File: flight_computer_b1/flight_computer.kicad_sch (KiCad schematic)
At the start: 11 parts, among them J1 DB25_Socket, J2 DB25_Socket, J3 Conn_01x03, J4 Screw_Terminal_01x02, J5 Pi Connector, J6 Conn_02x02_Odd_Even

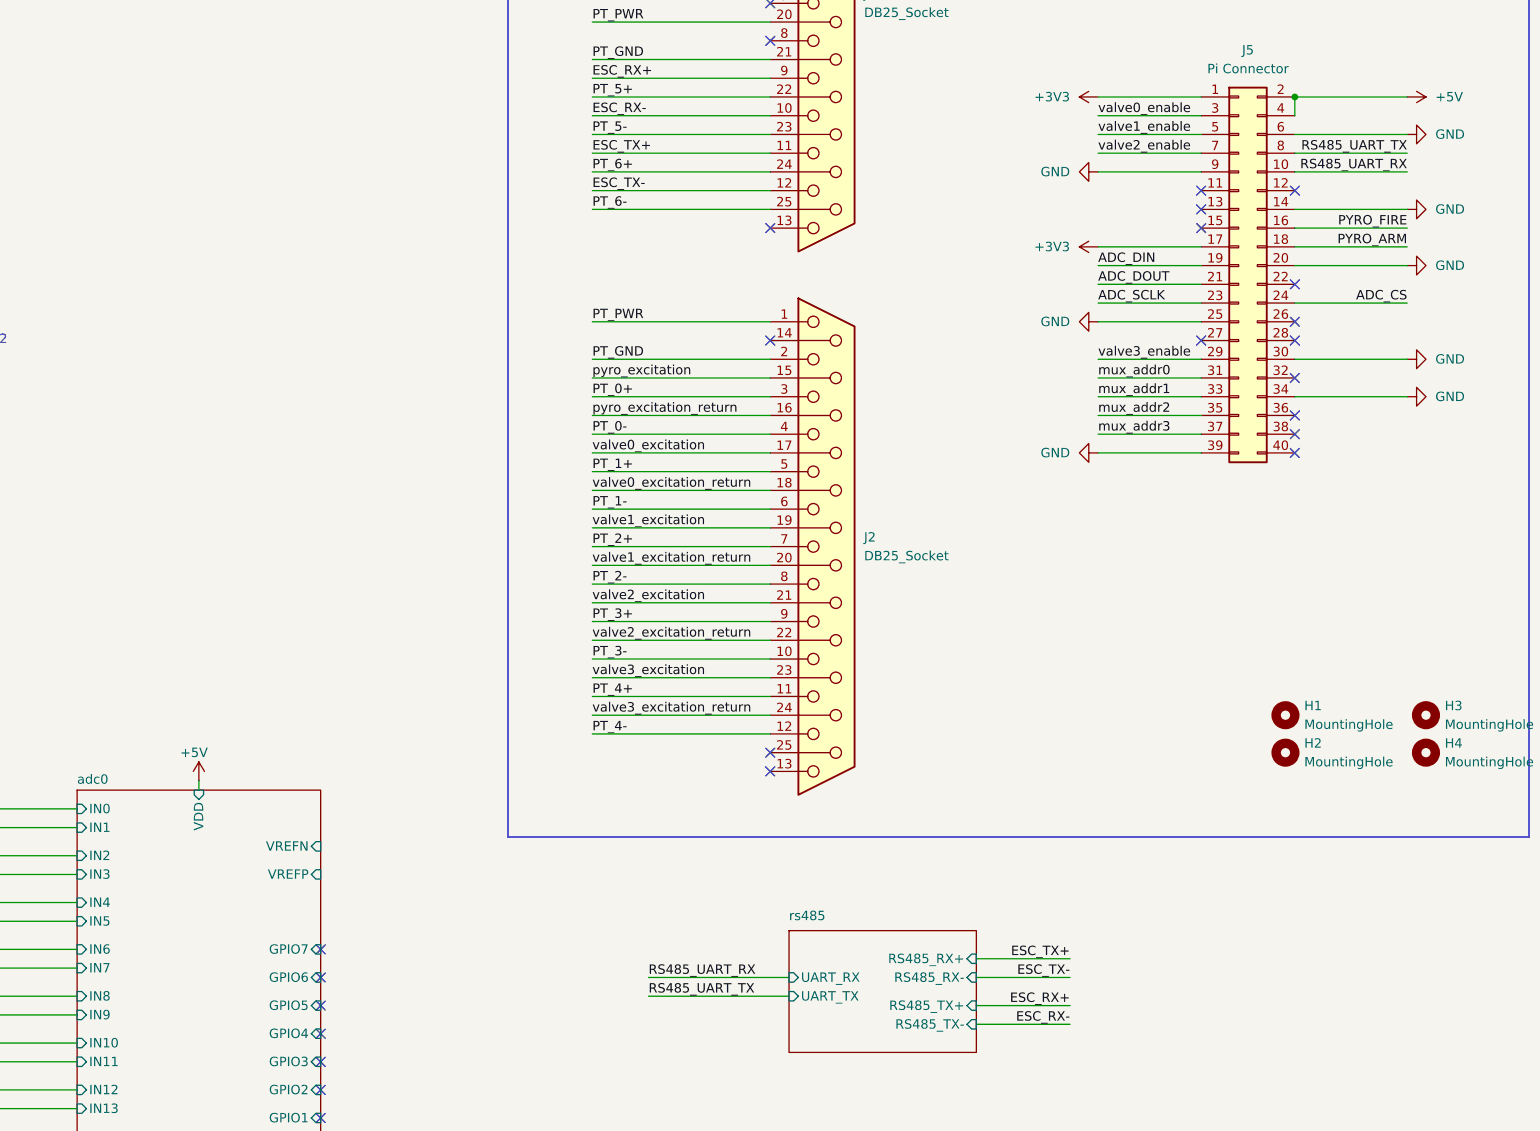
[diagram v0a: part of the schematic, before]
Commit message: flight computer: new pyro circuit
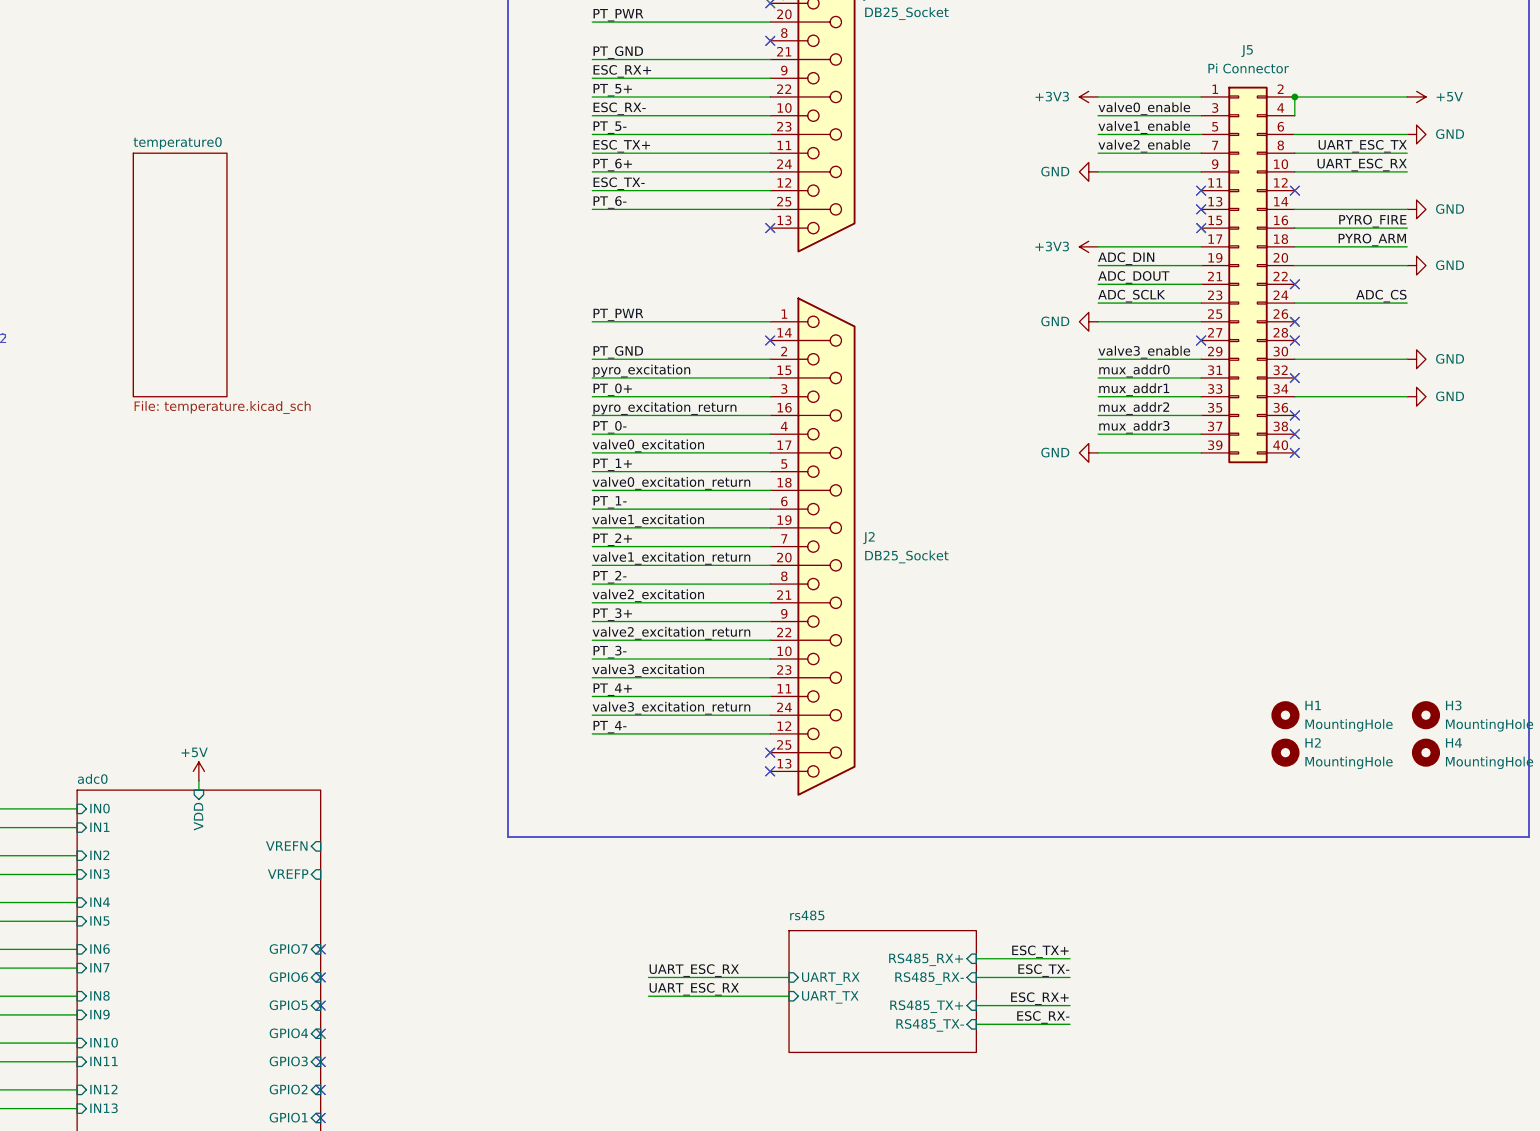
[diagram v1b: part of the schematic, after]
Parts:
- J4: DIGIKEY PART N (none) -> 277-6405-ND
- NT1: footprint (none) -> NetTie:NetTie-2_SMD_Pad0.5mm
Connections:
- net RS485_UART_RX renamed UART_ESC_RX
- net RS485_UART_TX renamed UART_ESC_TX
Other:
- added sheet temperature0 (temperature.kicad_sch)
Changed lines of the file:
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@@
 		)
 	)
-	(label "RS485_UART_RX"
+	(label "UART_ESC_RX"
 		(at 388.62 82.55 180)
 		(effects
@@
 		)
 	)
-	(label "RS485_UART_RX"
+	(label "UART_ESC_RX"
 		(at 285.75 191.77 0)
 		(effects
@@
 		)
 	)
-	(label "RS485_UART_TX"
+	(label "UART_ESC_TX"
 		(at 388.62 80.01 180)
 		(effects
@@
 		)
 	)
-	(label "RS485_UART_TX"
+	(label "UART_ESC_RX"
 		(at 285.75 194.31 0)
 		(effects
@@
 			)
 		)
-		(property "Footprint" ""
+		(property "Footprint" "NetTie:NetTie-2_SMD_Pad0.5mm"
 			(at 171.45 144.78 0)
 			(effects
@@
 			)
 		)
+		(property "DIGIKEY PART N" "277-6405-ND "
+			(at 355.6 24.13 0)
+			(effects
+				(font
+					(size 1.27 1.27)
+				)
+				(hide yes)
+			)
+		)
 		(pin "1"
 		)
@@
 				)
 			)
+		)
+	)
+	(sheet
+		(at 215.9 80.01)
+		(size 12.7 33.02)
+		(exclude_from_sim no)
+		(in_bom yes)
+		(on_board yes)
+		(dnp no)
+		(fields_autoplaced yes)
+		(stroke
+			(width 0.1524)
+			(type solid)
+		)
+		(fill
+			(color 0 0 0 0.0000)
+		)
+		(property "Sheetname" "temperature0"
+			(at 215.9 79.2984 0)
+			(effects
+				(font
+					(size 1.27 1.27)
+				)
+				(justify left bottom)
+			)
+		)
+		(property "Sheetfile" "temperature.kicad_sch"
+			(at 215.9 113.6146 0)
+			(effects
+				(font
+					(size 1.27 1.27)
+				)
+				(justify left top)
+			)
+		)
+		(instances
+			(project "flight_computer"
+				(path "/b71a7b79-cdb5-4e38-a72c-0daaa3474f05"
+					(page "20")
+				)
+			)

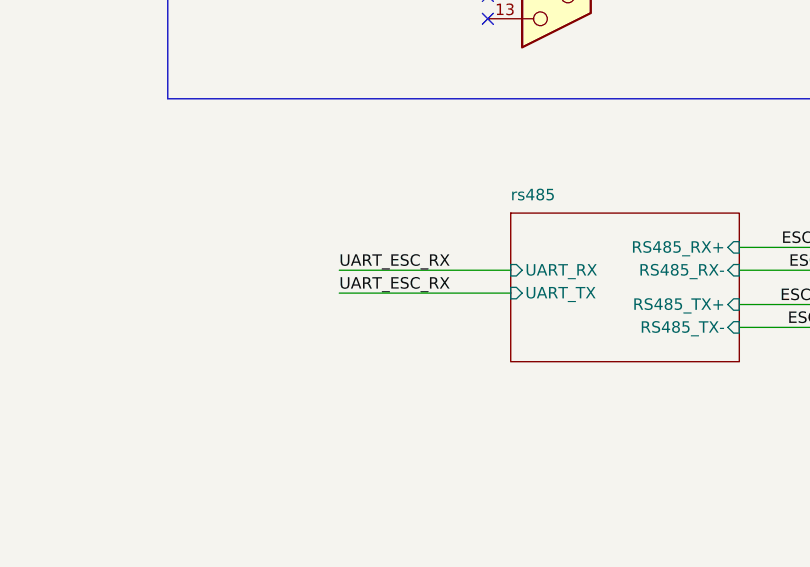
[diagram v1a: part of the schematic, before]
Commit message: flight computer: almost all routing done
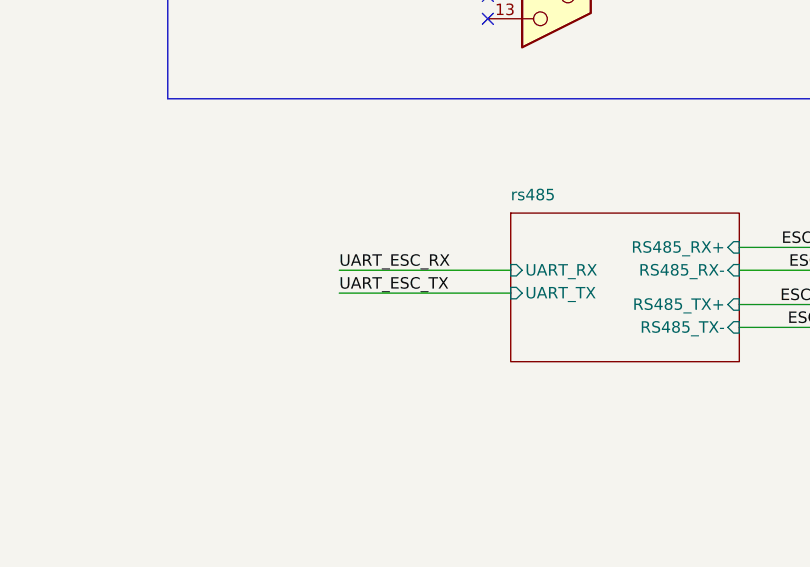
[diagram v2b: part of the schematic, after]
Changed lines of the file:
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@@
 		)
 	)
-	(label "UART_ESC_RX"
+	(label "UART_ESC_TX"
 		(at 285.75 194.31 0)
 		(effects

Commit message: block 1 fc tc updates
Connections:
- net mux_addr2: no longer J5.35 (Pin_35)
- net mux_addr3: no longer J5.37 (Pin_37)
- net TEMP_CS: now reaches J5.36 (Pin_36)
- net TEMP_DIN: now reaches J5.38 (Pin_38)
- net TEMP_SCLK: now reaches J5.40 (Pin_40)
- new net TEMP_DOUT: J5.35 (Pin_35)
- no-connect marks 46 -> 43
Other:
- sheet temperature0 ports: added CS, DIN, DOUT, GND, INTERRUPT, RTD1A, RTD1B, RTD1C, RTD2A, RTD2B, RTD2C, SCLK, TC1+, TC1-, TC2+, TC2-, TC3+, TC3-, TC4+, TC4-, VDD; removed none

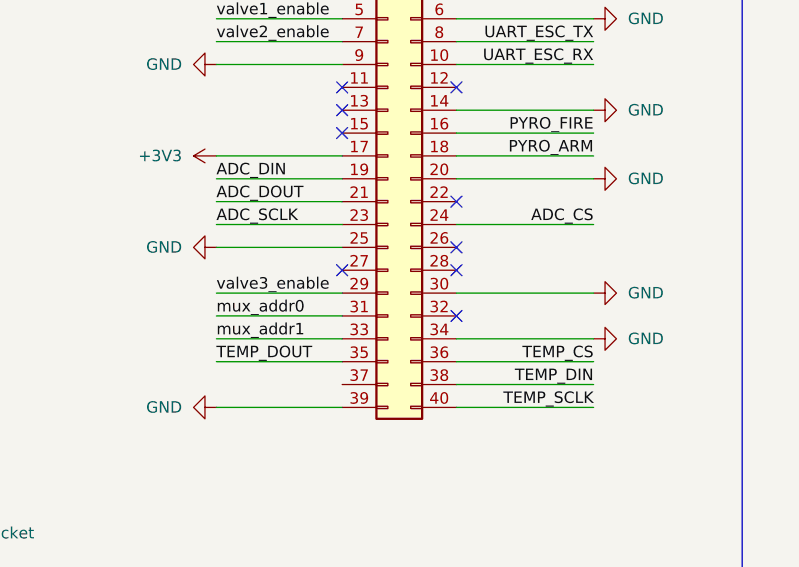
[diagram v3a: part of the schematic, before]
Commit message: routed traces for pi & fixed many DRC issues
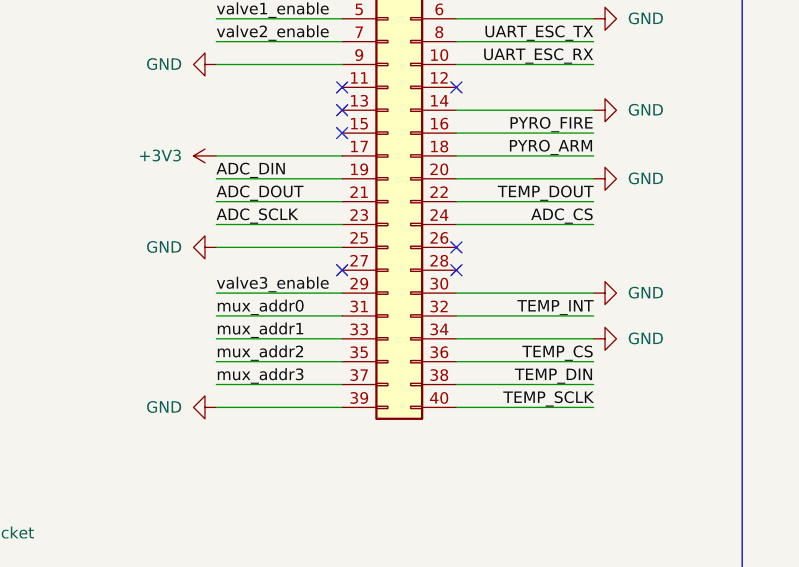
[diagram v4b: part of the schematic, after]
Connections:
- net TEMP_DOUT: now also J5.22 (Pin_22); no longer J5.35 (Pin_35)
- net TEMP_INT: now also J5.32 (Pin_32)
- net mux_addr2: now also J5.35 (Pin_35)
- net mux_addr3: now also J5.37 (Pin_37)
- no-connect marks 43 -> 41
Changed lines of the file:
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@@
-	)
-	(no_connect
-		(at 373.38 110.49)
 	)
 	(no_connect
 		(at 302.26 57.15)
-	)
-	(no_connect
-		(at 373.38 97.79)
 	)
 	(no_connect
@@
 	(wire
 		(pts
+			(xy 373.38 97.79) (xy 388.62 97.79)
+		)
+		(stroke
+			(width 0)
+			(type default)
+		)
+	)
+	(wire
+		(pts
 			(xy 209.55 100.33) (xy 199.39 100.33)
 		)
@@
 		(pts
 			(xy 43.18 24.13) (xy 17.78 24.13)
+		)
+		(stroke
+			(width 0)
+			(type default)
+		)
+	)
+	(wire
+		(pts
+			(xy 373.38 110.49) (xy 388.62 110.49)
+		)
+		(stroke
+			(width 0)
+			(type default)
+		)
+	)
+	(wire
+		(pts
+			(xy 346.71 118.11) (xy 360.68 118.11)
 		)
 		(stroke
@@
 		)
 	)
+	(label "TEMP_INT"
+		(at 388.62 110.49 180)
+		(effects
+			(font
+				(size 1.27 1.27)
+			)
+			(justify right bottom)
+		)
+	)
+	(label "TEMP_DOUT"
+		(at 388.62 97.79 180)
+		(effects
+			(font
+				(size 1.27 1.27)
+			)
+			(justify right bottom)
+		)
+	)
+	(label "mux_addr2"
+		(at 346.71 115.57 0)
+		(effects
+			(font
+				(size 1.27 1.27)
+			)
+			(justify left bottom)
+		)
+	)
 	(label "ADC_DIN"
 		(at 204.47 236.22 180)
@@
 		)
 	)
+	(label "mux_addr3"
+		(at 346.71 118.11 0)
+		(effects
+			(font
+				(size 1.27 1.27)
+			)
+			(justify left bottom)
+		)
+	)
 	(label "PT_0+"
 		(at 148.59 168.91 0)
@@
 		)
 	)
-	(label "TEMP_DOUT"
-		(at 346.71 115.57 0)
-		(effects
-			(font
-				(size 1.27 1.27)
-			)
-			(justify left bottom)
-		)
-	)
 	(label "PT_PWR"
 		(at 278.13 102.87 0)
@@
 		)
 	)
+	(label "TEMP_SCLK"
+		(at 388.62 120.65 180)
+		(effects
+			(font
+				(size 1.27 1.27)
+			)
+			(justify right bottom)
+		)
+	)
 	(label "RTD2C"
 		(at 199.39 67.31 0)
@@
 		)
 	)
-	(label "TEMP_SCLK"
-		(at 388.62 120.65 180)
-		(effects
-			(font
-				(size 1.27 1.27)
-			)
-			(justify right bottom)
-		)
-	)

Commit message: net updates
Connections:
- no-connect marks 41 -> 38
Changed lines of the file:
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@@
-	)
-	(no_connect
-		(at 302.26 59.69)
 	)
 	(no_connect
@@
 	)
 	(no_connect
-		(at 302.26 64.77)
-	)
-	(no_connect
 		(at 302.26 41.91)
 	)
@@
 	(no_connect
 		(at 373.38 105.41)
-	)
-	(no_connect
-		(at 302.26 57.15)
 	)
 	(no_connect
@@
 	(wire
 		(pts
+			(xy 278.13 64.77) (xy 302.26 64.77)
+		)
+		(stroke
+			(width 0)
+			(type default)
+		)
+	)
+	(wire
+		(pts
 			(xy 226.06 55.88) (xy 226.06 59.69)
 		)
@@
 	(wire
 		(pts
+			(xy 278.13 57.15) (xy 302.26 57.15)
+		)
+		(stroke
+			(width 0)
+			(type default)
+		)
+	)
+	(wire
+		(pts
 			(xy 373.38 120.65) (xy 388.62 120.65)
 		)
@@
 		(pts
 			(xy 90.17 222.25) (xy 109.22 222.25)
+		)
+		(stroke
+			(width 0)
+			(type default)
+		)
+	)
+	(wire
+		(pts
+			(xy 278.13 59.69) (xy 302.26 59.69)
 		)
 		(stroke
@@
 		(effects
 			(font
+				(size 1.27 1.27)
+			)
+			(justify left bottom)
+		)
+	)
+	(label "OX_RTDA"
+		(at 278.13 55.88 0)
+		(effects
+			(font

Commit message: net updates fr
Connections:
- net OX_RTD_UPPER_B: now reaches J1.18 (P18)
- net OX_RTD_LOWER_A: now reaches J1.19 (P19)
- net OX_RTD_UPPER_A: now reaches J1.5
- net OX_RTD_UPPER_C: now reaches J1.6
- net OX_RTD_LOWER_B: now reaches J1.7
- net OX_RTD_LOWER_C: now reaches J1.8
- no-connect marks 38 -> 35
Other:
- sheet temperature0 ports: added OX_RTD_LOWER_A, OX_RTD_LOWER_B, OX_RTD_LOWER_C, OX_RTD_UPPER_A, OX_RTD_UPPER_B, OX_RTD_UPPER_C; removed RTD1A, RTD1B, RTD1C, RTD2A, RTD2B, RTD2C

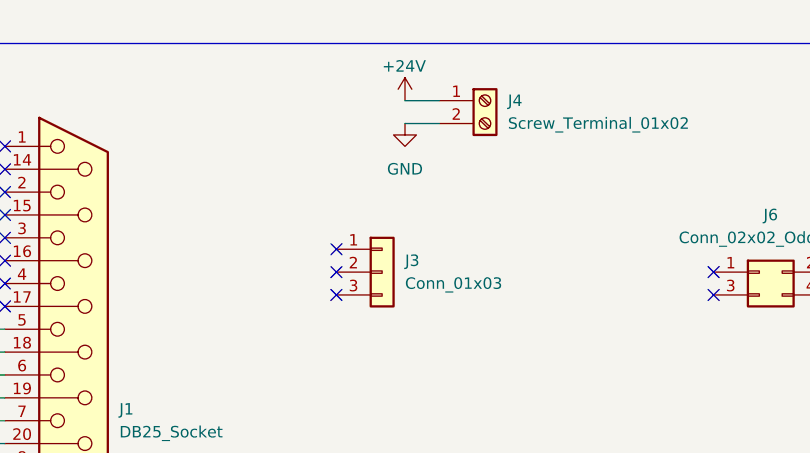
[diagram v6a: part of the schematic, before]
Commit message: routed pi traces, fixed all unavoidable DRC errors
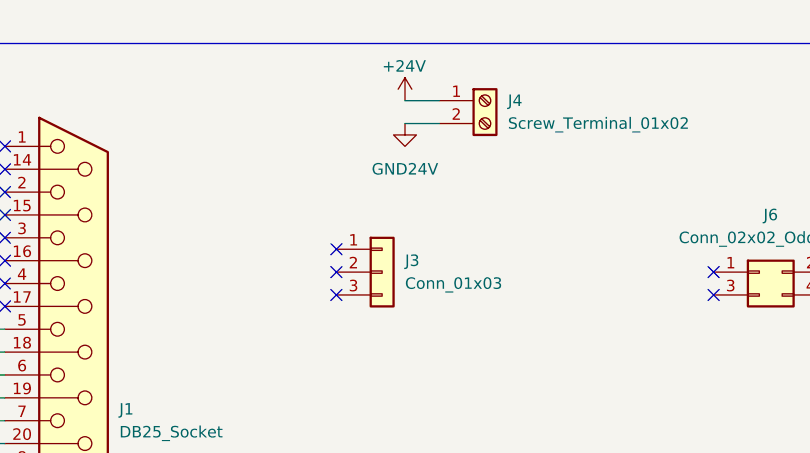
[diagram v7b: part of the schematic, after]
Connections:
- net GND: no longer J4.2 (Pin_2)
- new net GND24V: J4.2 (Pin_2)
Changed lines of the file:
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@@
 			)
 		)
-		(property "Value" "GND"
+		(property "Value" "GND24V"
 			(at 346.71 31.75 0)
 			(effects
